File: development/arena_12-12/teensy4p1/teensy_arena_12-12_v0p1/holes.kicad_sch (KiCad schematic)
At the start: 4 parts

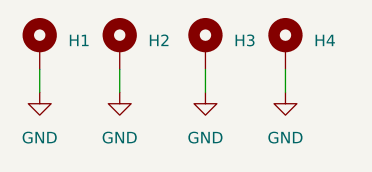
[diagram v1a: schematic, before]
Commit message: More work on schematic for 12-12 teensy arena.
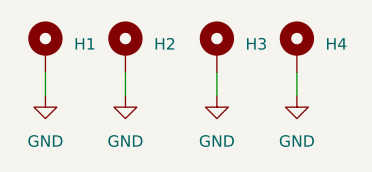
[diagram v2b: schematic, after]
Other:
- moved on the sheet: H1, H2, H3, H4
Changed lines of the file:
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@@
 	(wire
 		(pts
-			(xy 41.275 32.639) (xy 41.275 35.179)
+			(xy 41.91 33.02) (xy 41.91 35.56)
 		)
 		(stroke
@@
 	(wire
 		(pts
-			(xy 59.69 32.639) (xy 59.69 35.179)
+			(xy 60.96 33.02) (xy 60.96 35.56)
 		)
 		(stroke
@@
 	(wire
 		(pts
-			(xy 68.58 32.639) (xy 68.58 35.179)
+			(xy 69.85 33.02) (xy 69.85 35.56)
 		)
 		(stroke
@@
 	(wire
 		(pts
-			(xy 50.165 32.639) (xy 50.165 35.179)
+			(xy 50.8 33.02) (xy 50.8 35.56)
 		)
 		(stroke
@@
 	(symbol
 		(lib_id "power:GND")
-		(at 68.58 35.179 0)
+		(at 69.85 35.56 0)
 		(mirror y)
 		(unit 1)
@@
 		(fields_autoplaced yes)
 		(property "Reference" "#PWR011"
-			(at 68.58 41.529 0)
+			(at 69.85 41.91 0)
 			(effects
 				(font
@@
 		)
 		(property "Value" "GND"
-			(at 68.58 40.259 0)
+			(at 69.85 40.64 0)
 			(effects
 				(font
@@
 		)
 		(property "Footprint" ""
-			(at 68.58 35.179 0)
+			(at 69.85 35.56 0)
 			(effects
 				(font
@@
 		)
 		(property "Datasheet" ""
-			(at 68.58 35.179 0)
-			(effects
-				(font
-					(size 1.27 1.27)
-				)
-				(hide yes)
-			)
-		)
-		(property "Description" ""
-			(at 68.58 35.179 0)
+			(at 69.85 35.56 0)
+			(effects
+				(font
+					(size 1.27 1.27)
+				)
+				(hide yes)
+			)
+		)
+		(property "Description" ""
+			(at 69.85 35.56 0)
 			(effects
 				(font
@@
 	(symbol
 		(lib_id "Mechanical:MountingHole_Pad")
-		(at 50.165 30.099 0)
+		(at 50.8 30.48 0)
 		(unit 1)
 		(exclude_from_sim no)
@@
 		(dnp no)
 		(property "Reference" "H2"
-			(at 53.34 29.464 0)
+			(at 53.975 29.845 0)
 			(effects
 				(font
@@
 		)
 		(property "Value" "MountingHole_Pad"
-			(at 53.34 30.734 0)
+			(at 53.975 31.115 0)
 			(effects
 				(font
@@
 		)
 		(property "Footprint" "MountingHole:MountingHole_4.5mm_Pad"
-			(at 50.165 30.099 0)
+			(at 50.8 30.48 0)
 			(effects
 				(font
@@
 		)
 		(property "Datasheet" "~"
-			(at 50.165 30.099 0)
-			(effects
-				(font
-					(size 1.27 1.27)
-				)
-				(hide yes)
-			)
-		)
-		(property "Description" ""
-			(at 50.165 30.099 0)
+			(at 50.8 30.48 0)
+			(effects
+				(font
+					(size 1.27 1.27)
+				)
+				(hide yes)
+			)
+		)
+		(property "Description" ""
+			(at 50.8 30.48 0)
 			(effects
 				(font
@@
 	(symbol
 		(lib_id "power:GND")
-		(at 50.165 35.179 0)
+		(at 50.8 35.56 0)
 		(mirror y)
 		(unit 1)
@@
 		(fields_autoplaced yes)
 		(property "Reference" "#PWR09"
-			(at 50.165 41.529 0)
+			(at 50.8 41.91 0)
 			(effects
 				(font
@@
 		)
 		(property "Value" "GND"
-			(at 50.165 40.259 0)
+			(at 50.8 40.64 0)
 			(effects
 				(font
@@
 		)
 		(property "Footprint" ""
-			(at 50.165 35.179 0)
+			(at 50.8 35.56 0)
 			(effects
 				(font
@@
 		)
 		(property "Datasheet" ""
-			(at 50.165 35.179 0)
-			(effects
-				(font
-					(size 1.27 1.27)
-				)
-				(hide yes)
-			)
-		)
-		(property "Description" ""
-			(at 50.165 35.179 0)
+			(at 50.8 35.56 0)
+			(effects
+				(font
+					(size 1.27 1.27)
+				)
+				(hide yes)
+			)
+		)
+		(property "Description" ""
+			(at 50.8 35.56 0)
 			(effects
 				(font
@@
 	(symbol
 		(lib_id "power:GND")
-		(at 41.275 35.179 0)
+		(at 41.91 35.56 0)
 		(mirror y)
 		(unit 1)
@@
 		(fields_autoplaced yes)
 		(property "Reference" "#PWR08"
-			(at 41.275 41.529 0)
+			(at 41.91 41.91 0)
 			(effects
 				(font
@@
 		)
 		(property "Value" "GND"
-			(at 41.275 40.259 0)
+			(at 41.91 40.64 0)
 			(effects
 				(font
@@
 		)
 		(property "Footprint" ""
-			(at 41.275 35.179 0)
+			(at 41.91 35.56 0)
 			(effects
 				(font
@@
 		)
 		(property "Datasheet" ""
-			(at 41.275 35.179 0)
-			(effects
-				(font
-					(size 1.27 1.27)
-				)
-				(hide yes)
-			)
-		)
-		(property "Description" ""
-			(at 41.275 35.179 0)
+			(at 41.91 35.56 0)
+			(effects
+				(font
+					(size 1.27 1.27)
+				)
+				(hide yes)
+			)
+		)
+		(property "Description" ""
+			(at 41.91 35.56 0)
 			(effects
 				(font
@@
 	(symbol
 		(lib_id "Mechanical:MountingHole_Pad")
-		(at 59.69 30.099 0)
+		(at 60.96 30.48 0)
 		(unit 1)
 		(exclude_from_sim no)
@@
 		(fields_autoplaced yes)
 		(property "Reference" "H3"
-			(at 62.865 29.464 0)
+			(at 64.135 29.845 0)
 			(effects
 				(font
@@
 		)
 		(property "Value" "MountingHole_Pad"
-			(at 62.865 30.734 0)
+			(at 64.135 31.115 0)
 			(effects
 				(font
@@
 		)
 		(property "Footprint" "MountingHole:MountingHole_4.5mm_Pad"
-			(at 59.69 30.099 0)
+			(at 60.96 30.48 0)
 			(effects
 				(font
@@
 		)
 		(property "Datasheet" "~"
-			(at 59.69 30.099 0)
-			(effects
-				(font
-					(size 1.27 1.27)
-				)
-				(hide yes)
-			)
-		)
-		(property "Description" ""
-			(at 59.69 30.099 0)
+			(at 60.96 30.48 0)
+			(effects
+				(font
+					(size 1.27 1.27)
+				)
+				(hide yes)
+			)
+		)
+		(property "Description" ""
+			(at 60.96 30.48 0)
 			(effects
 				(font
@@
 	(symbol
 		(lib_id "Mechanical:MountingHole_Pad")
-		(at 41.275 30.099 0)
+		(at 41.91 30.48 0)
 		(unit 1)
 		(exclude_from_sim no)
@@
 		(fields_autoplaced yes)
 		(property "Reference" "H1"
-			(at 44.45 29.464 0)
+			(at 45.085 29.845 0)
 			(effects
 				(font
@@
 		)
 		(property "Value" "MountingHole_Pad"
-			(at 44.45 30.734 0)
+			(at 45.085 31.115 0)
 			(effects
 				(font
@@
 		)
 		(property "Footprint" "MountingHole:MountingHole_4.5mm_Pad"
-			(at 41.275 30.099 0)
+			(at 41.91 30.48 0)
 			(effects
 				(font
@@
 		)
 		(property "Datasheet" "~"
-			(at 41.275 30.099 0)
-			(effects
-				(font
-					(size 1.27 1.27)
-				)
-				(hide yes)
-			)
-		)
-		(property "Description" ""
-			(at 41.275 30.099 0)
+			(at 41.91 30.48 0)
+			(effects
+				(font
+					(size 1.27 1.27)
+				)
+				(hide yes)
+			)
+		)
+		(property "Description" ""
+			(at 41.91 30.48 0)
 			(effects
 				(font
@@
 	(symbol
 		(lib_id "power:GND")
-		(at 59.69 35.179 0)
+		(at 60.96 35.56 0)
 		(mirror y)
 		(unit 1)
@@
 		(fields_autoplaced yes)
 		(property "Reference" "#PWR010"
-			(at 59.69 41.529 0)
+			(at 60.96 41.91 0)
 			(effects
 				(font
@@
 		)
 		(property "Value" "GND"
-			(at 59.69 40.259 0)
+			(at 60.96 40.64 0)
 			(effects
 				(font
@@
 		)
 		(property "Footprint" ""
-			(at 59.69 35.179 0)
+			(at 60.96 35.56 0)
 			(effects
 				(font
@@
 		)
 		(property "Datasheet" ""
-			(at 59.69 35.179 0)
-			(effects
-				(font
-					(size 1.27 1.27)
-				)
-				(hide yes)
-			)
-		)
-		(property "Description" ""
-			(at 59.69 35.179 0)
+			(at 60.96 35.56 0)
+			(effects
+				(font
+					(size 1.27 1.27)
+				)
+				(hide yes)
+			)
+		)
+		(property "Description" ""
+			(at 60.96 35.56 0)
 			(effects
 				(font
@@
 	(symbol
 		(lib_id "Mechanical:MountingHole_Pad")
-		(at 68.58 30.099 0)
+		(at 69.85 30.48 0)
 		(unit 1)
 		(exclude_from_sim no)
@@
 		(fields_autoplaced yes)
 		(property "Reference" "H4"
-			(at 71.755 29.464 0)
+			(at 73.025 29.845 0)
 			(effects
 				(font
@@
 		)
 		(property "Value" "MountingHole_Pad"
-			(at 71.755 30.734 0)
+			(at 73.025 31.115 0)
 			(effects
 				(font
@@
 		)
 		(property "Footprint" "MountingHole:MountingHole_4.5mm_Pad"
-			(at 68.58 30.099 0)
+			(at 69.85 30.48 0)
 			(effects
 				(font
@@
 		)
 		(property "Datasheet" "~"
-			(at 68.58 30.099 0)
-			(effects
-				(font
-					(size 1.27 1.27)
-				)
-				(hide yes)
-			)
-		)
-		(property "Description" ""
-			(at 68.58 30.099 0)
-			(effects
-				(font
+			(at 69.85 30.48 0)
+			(effects
+				(font
+					(size 1.27 1.27)
+				)
+				(hide yes)
+			)
+		)
+		(property "Description" ""
+			(at 69.85 30.48 0)
+			(effects
+				(font
